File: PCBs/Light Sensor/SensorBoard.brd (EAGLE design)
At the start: 69.8 x 56.8 mm, 21 parts, among them J1 AVR_SPI_PRG_6PTH

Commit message: Working layout
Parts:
- removed JP1: M02PTH, SparkFun-Connectors:1X02
- removed U$2, U$6: PINHD-1X10, adafruit:1X10-BIG
- added C1, C2, C3, C4, C5: (no value), SparkFun-Capacitors:1210
- added STANDOFF1, STANDOFF2, STANDOFF3: STAND-OFF, SparkFun-Electromechanical:STAND-OFF
- added TINY, XBEE: FTDI_DEVICE, SparkFun-Connectors:FTDI_DEVICE_SIDE
- U$1: value OPT101SMD -> OPT101TH; device MyLibrary:PDSO-U8 -> MyLibrary:DIL08
- U$4: value ATTINY85SMD -> TINY85-20-DIP; device MyLibrary:SO08 -> SparkFun-DigitalIC:DIP08
- moved MIC2920 49.5 mm to (63.8, 45.5), flipped to the bottom, turned to 0 degrees
- moved JP2 35.6 mm to (36.8, 53.6), turned to 180 degrees
- moved U$3 35.2 mm to (8.38, 44.7), turned to 270 degrees
- moved JP3 33.8 mm to (30.7, 53.6), turned to 180 degrees
- moved U$1 20.9 mm to (7.62, 35.8), turned to 270 degrees
- moved R2 19.3 mm to (38.9, 23.1), turned to 0 degrees
- moved J1 10.6 mm to (42.7, 4.83)
- moved R1 9.60 mm to (21.6, 51.6), turned to 90 degrees
- moved JP4 6.35 mm to (12.7, 52.1)
- moved U$7 2.16 mm to (52.5, 41.4), flipped to the top, turned to 90 degrees
- moved U$4 1.98 mm to (30.5, 35.8)
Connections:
- removed net MISO/TINY_TX: J1.1, U$4.6, U1.11
- removed net MOSI/TINY_RX: J1.4, U$4.5, U1.10
- removed net N$3: U$2.4, U$6.3
- removed net N$4: R2.P$1, U$2.1, U$2.10, U$2.5, U$6.1, U$6.10, U$6.5
- removed net N$5: JP1.2, U1.8
- removed net RESET: J1.5, U$4.1, U1.12
- removed net TINY_DTR: U$4.3, U1.13
- removed net XBEE_RESET: U$5.5, U1.3
- new net MISO/TINY_RX: J1.1, TINY.P$2, U$4.6, U1.11, XBEE.P$3
- new net MOSI/TINY_TX: J1.4, TINY.P$3, U$4.5, U1.10, XBEE.P$2
- new net RST/TINY_DTR: J1.5, U$4.1, U1.13
- net 3.3V: now also C2.1, C3.1, C4.1, C5.1
- net 5V: now also C1.1
- net APDS_9008: now also U$4.3; no longer U$4.2
- net GND: now also C1.2, C2.2, C3.2, C4.2, C5.2, TINY.P$6, XBEE.P$6; no longer JP1.1, U$2.7, U$6.7
- net N$2: now also R2.P$1, TINY.P$4, XBEE.P$4; no longer U$2.3, U$6.4
- net OPT_101: now also U$4.2; no longer U$4.7
- net SCK: now also U$4.7
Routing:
- net GND: track 0.00 -> 262.9 mm
- net 5V: track 0.00 -> 169.3 mm, vias 0 -> 2
- net 3.3V: track 0.00 -> 133.4 mm
- net MOSI/TINY_TX: track 0.00 -> 62.9 mm, vias 0 -> 1
- net RST/TINY_DTR: track 0.00 -> 60.9 mm
- net MISO/TINY_RX: track 0.00 -> 60.6 mm, vias 0 -> 1
- net OPT_101: track 0.00 -> 31.1 mm
- net APDS_9008: track 0.00 -> 31.1 mm
- net SCK: track 0.00 -> 30.6 mm, vias 0 -> 1
- net N$1: track 0.00 -> 13.7 mm
- net N$2: track 0.00 -> 12.0 mm
- net XBEE_TX: track 0.00 -> 7.86 mm
- net XBEE_DTR: track 0.00 -> 7.69 mm
- net XBEE_RX: track 0.00 -> 7.55 mm
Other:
- board text added: "ATTINY DEBUG"
- board text added: "PROGRAMMER"
- board text added: "XBEE DEBUG"
- board text removed: "PROCESSOR SERIAL"
- board text removed: "PROG"
- board text removed: "USB POWER"
- board text removed: "XBEE SERIAL"

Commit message: Unrouted
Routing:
- net GND: track 262.9 -> 7.62 mm
- net 5V: track 169.3 -> 5.08 mm, vias 2 -> 0
- net 3.3V: track 133.4 -> 5.44 mm
- net MOSI/TINY_TX: track 62.9 -> 0.00 mm, vias 1 -> 0
- net RST/TINY_DTR: track 60.9 -> 0.00 mm
- net MISO/TINY_RX: track 60.6 -> 0.00 mm, vias 1 -> 0
- net OPT_101: track 31.1 -> 0.00 mm
- net APDS_9008: track 31.1 -> 0.00 mm
- net SCK: track 30.6 -> 0.00 mm, vias 1 -> 0
- net N$1: track 13.7 -> 0.00 mm
- net N$2: track 12.0 -> 0.00 mm
- net XBEE_TX: track 7.86 -> 0.00 mm
- net XBEE_DTR: track 7.69 -> 0.00 mm
- net XBEE_RX: track 7.55 -> 0.00 mm

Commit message: Version taped out for rev A
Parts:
- added JP1: M021X02_NO_SILK, SparkFun-Connectors:1X02_NO_SILK
- U1: device SparkFun-DigitalIC:SO14 -> MyLibrary:SO14
- moved MIC2920 7.87 mm to (63.8, 37.6), turned to 90 degrees
- moved C1 0.76 mm to (21.8, 35.8)
- moved STANDOFF3 0.76 mm to (2.54, 53.6)
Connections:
- net GND: now also JP1.2
- net N$1: now also JP1.1
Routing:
- net GND: track 7.62 -> 270.4 mm, vias 0 -> 1
- net 5V: track 5.08 -> 164.8 mm, vias 0 -> 2
- net 3.3V: track 5.44 -> 142.7 mm, vias 0 -> 5
- net RST/TINY_DTR: track 0.00 -> 71.4 mm
- net MOSI/TINY_TX: track 0.00 -> 70.4 mm
- net MISO/TINY_RX: track 0.00 -> 58.3 mm, vias 0 -> 1
- net SCK: track 0.00 -> 42.6 mm
- net OPT_101: track 0.00 -> 31.0 mm
- net N$1: track 0.00 -> 26.5 mm, vias 0 -> 1
- net APDS_9008: track 0.00 -> 21.7 mm
- net N$2: track 0.00 -> 12.0 mm
- net XBEE_TX: track 0.00 -> 8.15 mm
- net XBEE_DTR: track 0.00 -> 7.53 mm
- net XBEE_RX: track 0.00 -> 7.35 mm
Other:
- board size 69.8 x 56.8 mm -> 70.6 x 56.8 mm
- board text added: "3.3V REGULATOR"
- board text added: "ATTINY85"
- board text added: "Autonomous Light Sensor"
- board text added: "Cabrillo Robotics Club"
- board text added: "DISCHARGE"
- board text added: "IR"
- board text added: "MM - 12192014 - A"
- board text added: "SOLAR POWER"
- board text added: "SUPERCAPACITOR"
- board text added: "USB POWER"
- board text added: "Visible"
- board text added: "XBEE"
- board text removed: "SOLAR"

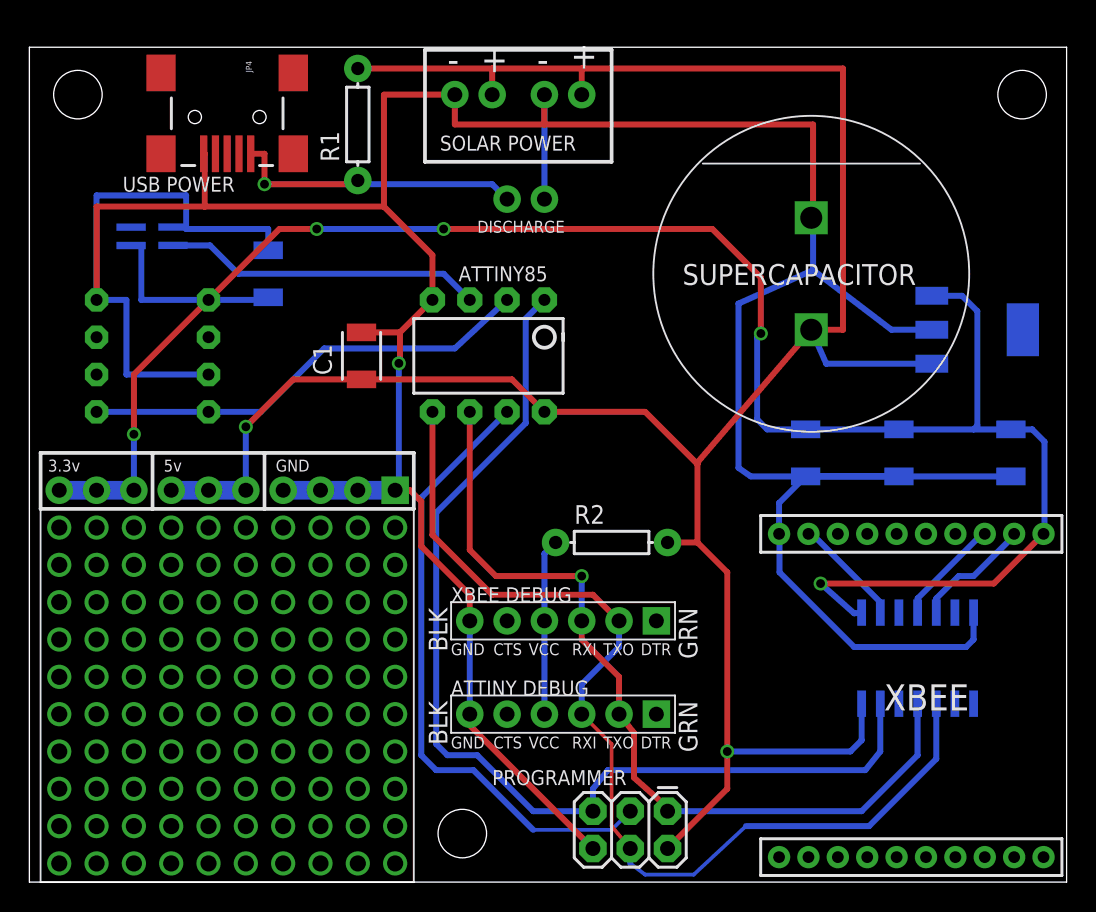
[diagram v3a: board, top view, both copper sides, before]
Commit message: Initial relayout for the new components
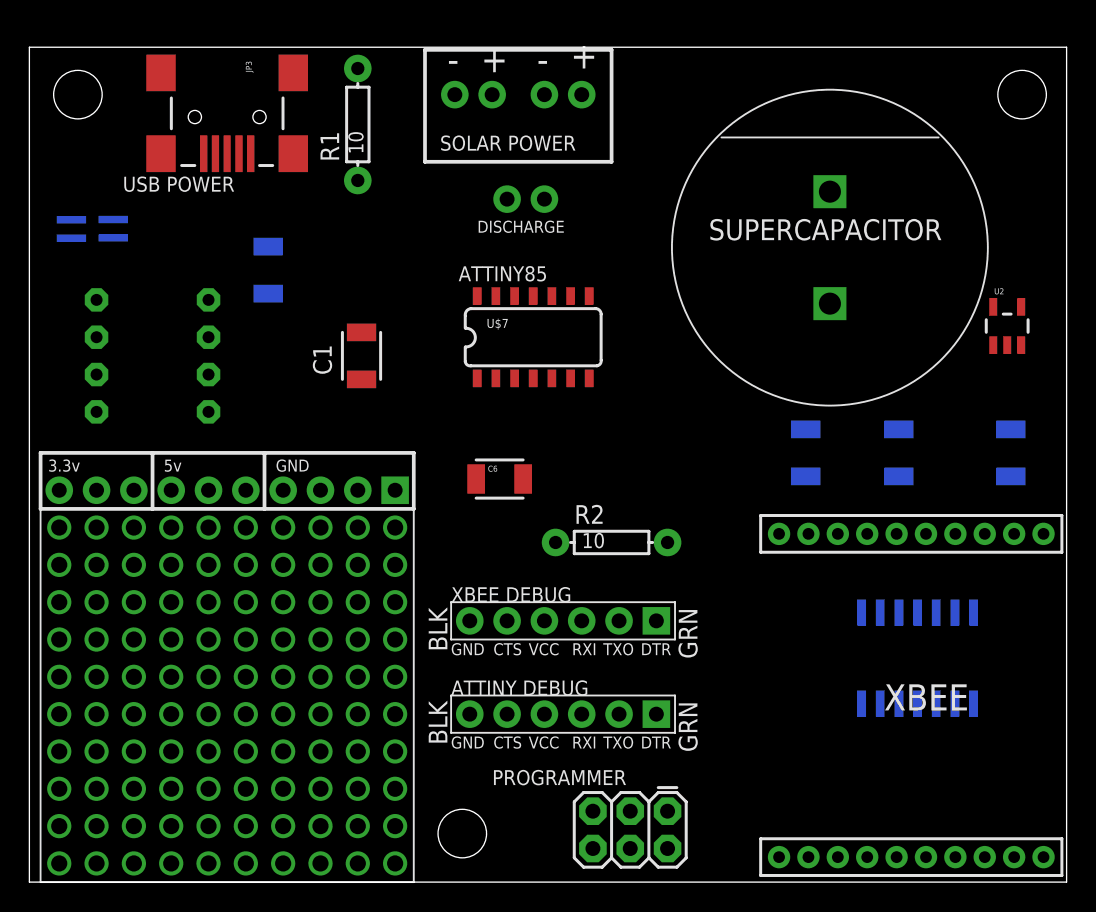
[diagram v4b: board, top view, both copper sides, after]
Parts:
- removed MIC2920: V_REG_MIC2920, SparkFun-PowerIC:SOT223
- removed U$8: PROTOAREA-10X10, MyLibrary:PROTOAREA-10X10
- added C6: 470pF, SparkFun-Capacitors:1210
- added U$2: APDS-9008, MyLibrary:APDS-9008
- added U2: MIC5219 3.3V, SparkFun-PowerIC:SOT23-5
- C1, C5: value (none) -> 0.1uf
- C2: value (none) -> 8.2pf
- C3: value (none) -> 1.0uf
- C4: value (none) -> 10uf
- JP3: value M021X02_NO_SILK -> USBSMD; device SparkFun-Connectors:1X02_NO_SILK -> SparkFun-Connectors:USB-MINIB
- JP4: value USBSMD -> M021X02_NO_SILK; device SparkFun-Connectors:USB-MINIB -> SparkFun-Connectors:1X02_NO_SILK
- R1, R2: value (none) -> 10
- U$1: value OPT101TH -> FYD0H225ZF; device MyLibrary:DIL08 -> MyLibrary:SUPERCAP-28.5
- U$3: value APDS-9008 -> PROTOAREA-10X10; device MyLibrary:APDS-9008 -> MyLibrary:PROTOAREA-10X10
- U$4: value TINY85-20-DIP -> OPT101TH; device SparkFun-DigitalIC:DIP08 -> MyLibrary:DIL08
- U$7: value FYD0H225ZF -> ATTINY84; device MyLibrary:SUPERCAP-28.5 -> SparkFun-DigitalIC:SO14
- moved U$1 46.7 mm to (53.7, 43.2), flipped to the top, turned to 90 degrees
- moved U$3 44.0 mm to (1.27, 1.27), flipped to the top, turned to 0 degrees
- moved U$4 22.9 mm to (7.62, 35.8), flipped to the bottom, turned to 270 degrees
- moved JP4 19.9 mm to (31.8, 46.5), turned to 0 degrees
- moved U$7 19.4 mm to (33.5, 37.1), turned to 0 degrees
- moved JP3 18.1 mm to (12.7, 52.1), turned to 270 degrees
- moved JP1 8.74 mm to (36.8, 53.6), turned to 180 degrees
- moved JP2 6.10 mm to (30.7, 53.6)
- moved C5 0.25 mm to (15.5, 41.7)
- renumbered U$5 to U$6
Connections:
- new net 3.3V_ENABLE: U$7.6, U2.3
- new net AUX_ANALOG: U$7.13
- new net MISO: J1.1, U$7.8
- new net MOSI: J1.4, U$7.7
- new net N$3: C6.1, U2.4
- new net RADIO_OFF: U$7.5
- new net RST: J1.5, U$7.4
- new net TINY_RX: U$7.2
- new net TINY_TX: U$7.3
- net 3.3V: now also U$2.1, U$4.1, U$7.12, U2.5; no longer MIC2920.3, U$1.1, U$3.1
- net 5V: now also JP1.1, U$1.+, U$7.1, U2.1; no longer JP3.1, MIC2920.1, U$4.8, U$7.+
- net APDS_9008: now also U$2.6, U$7.11; no longer U$3.6, U$4.3
- net GND: now also C6.2, JP3.GND, JP4.2, U$1.-, U$2.4, U$4.3, U$4.8, U$7.14, U2.2; no longer JP3.2, JP4.GND, MIC2920.2, U$1.3, U$1.8, U$3.4, U$4.4, U$7.-
- net MISO/TINY_RX: no longer J1.1, U$4.6
- net MOSI/TINY_TX: no longer J1.4, U$4.5
- net N$1: now also JP3.VBUS, JP4.1; no longer JP1.1, JP4.VBUS
- net OPT_101: now also U$4.4, U$4.5, U$7.10; no longer U$1.4, U$1.5, U$4.2
- net RST/TINY_DTR: no longer J1.5, U$4.1
- net SCK: now also U$7.9; no longer U$4.7
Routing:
- net GND: track 270.4 -> 0.00 mm, vias 1 -> 0
- net 5V: track 164.8 -> 0.00 mm, vias 2 -> 0
- net 3.3V: track 142.7 -> 0.00 mm, vias 5 -> 0
- net RST/TINY_DTR: track 71.4 -> 0.00 mm
- net MOSI/TINY_TX: track 70.4 -> 0.00 mm
- net MISO/TINY_RX: track 58.3 -> 0.00 mm, vias 1 -> 0
- net SCK: track 42.6 -> 0.00 mm
- net OPT_101: track 31.0 -> 0.00 mm
- net N$1: track 26.5 -> 0.00 mm, vias 1 -> 0
- net APDS_9008: track 21.7 -> 0.00 mm
- net N$2: track 12.0 -> 0.00 mm
- net XBEE_TX: track 8.15 -> 0.00 mm
- net XBEE_DTR: track 7.53 -> 0.00 mm
- net XBEE_RX: track 7.35 -> 0.00 mm

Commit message: Working on updates
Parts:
- removed U1: (no value), MyLibrary:SO14
- added C7, C8: 0.1uf, SparkFun-Capacitors:1210
- added R3: 1k, rcl:R1210
- added R4: (no value), rcl:R1210
- added U$5, U$8: SN74LVC2T45, MyLibrary:DCT-R-PDSO-G8
- moved U2 21.6 mm to (44.2, 36.8), flipped to the bottom, turned to 180 degrees
- moved U$1 1.70 mm to (55.2, 43.9)
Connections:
- removed net MISO/TINY_RX: TINY.P$2, U1.11, XBEE.P$3
- removed net MOSI/TINY_TX: TINY.P$3, U1.10, XBEE.P$2
- removed net RST/TINY_DTR: U1.13
- new net /XBEE_DEBUG: R3.2, R4.2, U$5.P$5
- net 3.3V: now also C7.1, U$5.P$8, U$8.P$8; no longer U1.1
- net 5V: now also C8.1, R3.1, U$5.P$1, U$8.P$1; no longer U1.14
- net GND: now also C7.2, C8.2, U$5.P$4, U$8.P$4, U$8.P$5; no longer U1.7, XBEE.P$6
- net N$2: no longer XBEE.P$4
- net RST: now also R4.1
- net TINY_RX: now also TINY.P$2
- net TINY_TX: now also TINY.P$3
- net XBEE_DTR: now also U$5.P$7, XBEE.P$1; no longer U1.2
- net XBEE_RX: now also U$5.P$6, XBEE.P$2; no longer U1.4
- net XBEE_TX: now also U$8.P$7, XBEE.P$3; no longer U1.5

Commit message: Incremental updates
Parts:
- removed R2: 10, SparkFun-Passives:AXIAL-0.3
- added R5: 1k, rcl:R1210
- R4: value (none) -> 1k
- moved R4 118.0 mm to (65.8, 35.6), flipped to the bottom
- moved R3 92.7 mm to (45.0, 26.2), turned to 180 degrees
- moved C6 29.0 mm to (50.0, 49.5), flipped to the bottom, turned to 90 degrees
- moved C2 26.8 mm to (60.5, 3.05), turned to 0 degrees
- moved C4 21.5 mm to (60.5, 9.40), turned to 0 degrees
- moved C8 17.8 mm to (53.6, 24.6), turned to 180 degrees
- moved U$5 16.7 mm to (50.5, 29.5), turned to 90 degrees
- moved U$8 14.3 mm to (61.0, 24.6), turned to 90 degrees
- moved U$6 12.8 mm to (57.4, 21.6), turned to 180 degrees
- moved U2 12.7 mm to (43.9, 49.5)
- moved C3 11.4 mm to (60.5, 18.0), turned to 0 degrees
- moved C7 11.2 mm to (61.0, 30.5), turned to 180 degrees
- moved TINY 9.67 mm to (35.1, 21.1)
- moved XBEE 6.14 mm to (34.8, 11.7)
- moved C5 6.04 mm to (9.91, 43.9)
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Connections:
- removed net N$1: JP3.VBUS, JP4.1, R1.P$1
- removed net N$2: R2.P$1, TINY.P$4
- new net VCC: JP3.VBUS, JP4.1, R1.P$1, TINY.P$4, XBEE.P$4
- net /XBEE_DEBUG: now also R5.1, XBEE.P$1; no longer R4.2
- net 3.3V: now also R4.2
- net 5V: no longer R2.P$2
- net GND: now also XBEE.P$6
- net RADIO_OFF: now also U$5.P$2
- net RST: now also R5.2; no longer R4.1
- net TINY_RX: now also U$8.P$2
- net TINY_TX: now also U$5.P$3
- net XBEE_DTR: now also R4.1; no longer XBEE.P$1
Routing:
- net GND: track 0.00 -> 258.0 mm, vias 0 -> 4
- net 3.3V: track 0.00 -> 178.4 mm, vias 0 -> 3
- net 5V: track 0.00 -> 173.8 mm, vias 0 -> 3
- net XBEE_RX: track 0.00 -> 62.5 mm, vias 0 -> 1
- net XBEE_TX: track 0.00 -> 61.5 mm, vias 0 -> 1
- net VCC: track 0.00 -> 54.7 mm
- net MISO: track 0.00 -> 43.2 mm
- net SCK: track 0.00 -> 41.9 mm
- net TINY_RX: track 0.00 -> 40.9 mm, vias 0 -> 1
- net RST: track 0.00 -> 38.9 mm, vias 0 -> 2
- net TINY_TX: track 0.00 -> 36.5 mm, vias 0 -> 1
- net MOSI: track 0.00 -> 35.8 mm, vias 0 -> 1
- net /XBEE_DEBUG: track 0.00 -> 35.3 mm, vias 0 -> 1
- net XBEE_DTR: track 0.00 -> 32.6 mm, vias 0 -> 1
- net 3.3V_ENABLE: track 0.00 -> 30.5 mm, vias 0 -> 1
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
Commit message: Still routing and placing
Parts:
- U$6: value XBEE-1B1 -> XBEE-2B1; device MyLibrary:XBEE-1 -> SparkFun-RF:XBEE-1
- moved C3 8.30 mm to (63.8, 10.4), turned to 90 degrees
- moved C2 8.29 mm to (56.6, 10.4), turned to 90 degrees
- moved C6 8.19 mm to (46.0, 42.4)
- moved U2 7.33 mm to (42.2, 42.4)
- moved JP4 5.49 mm to (28.7, 51.1), turned to 90 degrees
- moved R3 5.48 mm to (43.7, 31.5)
- moved R5 4.50 mm to (38.9, 26.7)
- moved JP2 4.32 mm to (35.1, 53.6)
- moved JP1 3.81 mm to (40.6, 53.6)
- moved R1 3.05 mm to (24.6, 51.6)
- moved JP3 3.05 mm to (15.7, 52.1)
- moved U$4 2.84 mm to (12.7, 36.8)
- moved R4 2.81 mm to (63.0, 35.3)
- moved C5 2.34 mm to (8.13, 45.5)
- moved U$2 1.48 mm to (3.05, 47.2)
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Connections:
- net 3.3V: now also U$7.13; no longer U$7.12
- net AUX_ANALOG: now also U$7.12; no longer U$7.13
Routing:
- net GND: track 258.0 -> 162.9 mm, vias 4 -> 1
- net 3.3V: track 178.4 -> 89.8 mm, vias 3 -> 2
- net 5V: track 173.8 -> 92.0 mm, vias 3 -> 1
- net XBEE_RX: track 62.5 -> 0.00 mm, vias 1 -> 0
- net XBEE_TX: track 61.5 -> 0.00 mm, vias 1 -> 0
- net MISO: track 43.2 -> 0.00 mm
- net SCK: track 41.9 -> 0.00 mm
- net TINY_RX: track 40.9 -> 0.00 mm, vias 1 -> 0
- net VCC: track 54.7 -> 15.0 mm
- net RST: track 38.9 -> 0.00 mm, vias 2 -> 0
- net TINY_TX: track 36.5 -> 0.00 mm, vias 1 -> 0
- net MOSI: track 35.8 -> 0.00 mm, vias 1 -> 0
- net /XBEE_DEBUG: track 35.3 -> 0.38 mm, vias 1 -> 0
- net XBEE_DTR: track 32.6 -> 0.00 mm, vias 1 -> 0
- net 3.3V_ENABLE: track 30.5 -> 0.00 mm, vias 1 -> 0
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- added copper zone on layer 16, net 3.3V
- added copper zone on layer 16, net GND

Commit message: Almost finished with layout
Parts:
- added R2: 1k, rcl:R1210
- moved STANDOFF2 73.2 mm to (-7.62, 66.8)
- moved STANDOFF1 68.3 mm to (-0.25, 66.8)
- moved JP3 52.5 mm to (41.1, 6.10), turned to 90 degrees
- moved JP2 44.1 mm to (68.6, 24.9), turned to 270 degrees
- moved R1 41.2 mm to (39.6, 13.2), turned to 0 degrees
- moved C3 38.7 mm to (51.1, 47.0), turned to 270 degrees
- moved JP1 38.3 mm to (66.0, 24.9), turned to 270 degrees
- moved C2 36.6 mm to (54.6, 47.0), turned to 270 degrees
- moved C4 36.6 mm to (58.2, 47.0), turned to 270 degrees
- moved JP4 36.0 mm to (38.1, 16.3), turned to 0 degrees
- moved C8 35.4 mm to (31.2, 52.1), flipped to the top, turned to 270 degrees
- moved C7 33.7 mm to (35.1, 52.1), flipped to the top, turned to 270 degrees
- moved U$1 33.6 mm to (58.9, 10.8)
- moved U$8 33.1 mm to (37.1, 47.5), flipped to the top, turned to 270 degrees
- moved U$5 23.1 mm to (32.5, 43.9), flipped to the top, turned to 180 degrees
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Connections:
- net 3.3V_ENABLE: now also R2.1
- net 5V: now also R2.2
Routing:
- net GND: track 162.9 -> 50.0 mm, vias 1 -> 2
- net 3.3V: track 89.8 -> 108.1 mm, vias 2 -> 1
- net 5V: track 92.0 -> 110.1 mm, vias 1 -> 0
- net VCC: track 15.0 -> 23.5 mm
- net 3.3V_ENABLE: track 0.00 -> 7.04 mm
- net N$3: track 2.98 -> 3.63 mm
